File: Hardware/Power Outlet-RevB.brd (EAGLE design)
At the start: 138.4 x 100 mm, 38 parts, among them IC1 ATMega 328p-pu, IC2 ULN2003AD, K1 G5LE, K2 G5LE, Q1 8MHz, X1 VIN, X2 VOUT2, X3 VOUT1, X7 EARTH

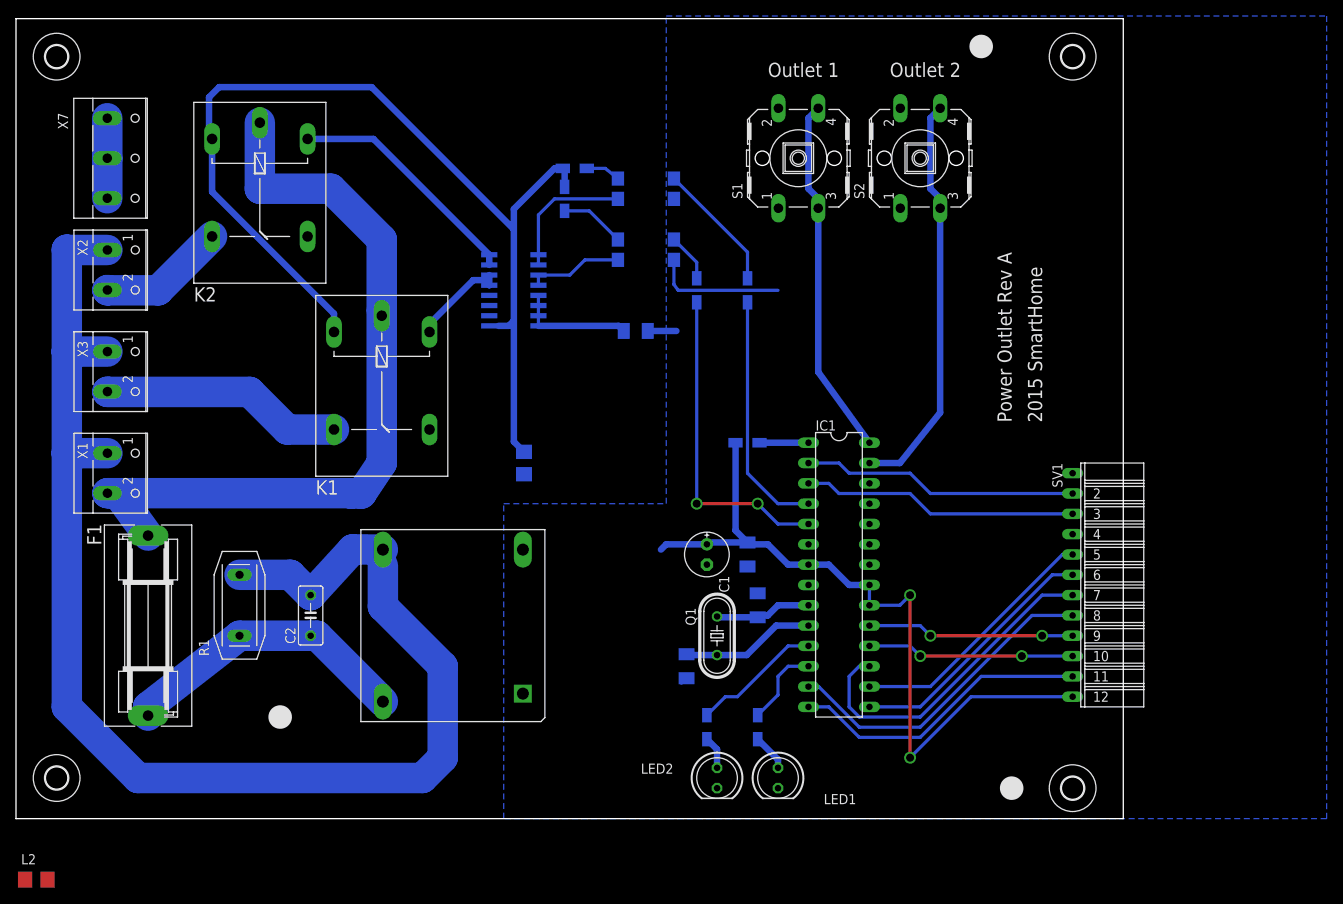
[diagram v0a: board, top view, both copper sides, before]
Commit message: updated wrong capacitor footprint, removed isolation cap as causes circuit not to function.
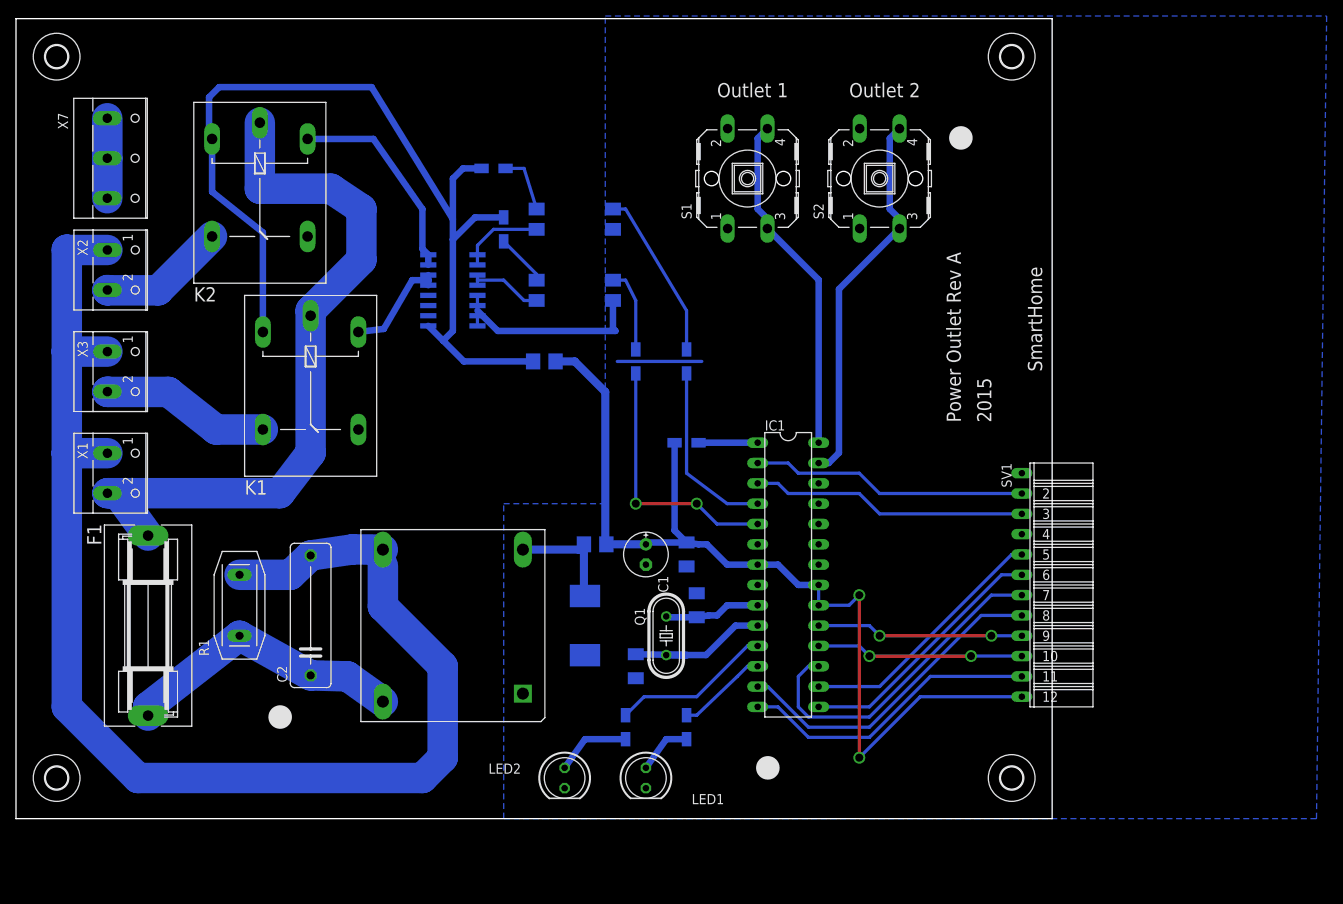
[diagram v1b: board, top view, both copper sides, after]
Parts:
- removed C6: 1n/2Kv, rcl:C1206K
- added D1: (no value), diode:SMC
- C2: device rcl:C050-030X075 -> rcl:C150-054X183
- OK1, OK2: device optocoupler:SMD4 -> optocoupler:DIL4-SMD
- moved L2 81.5 mm to (72.4, 34.3), flipped to the bottom
- moved LED2 19.0 mm to (68.6, 5.08)
- moved LED1 16.5 mm to (78.7, 5.08)
- moved L1 13.0 mm to (66.0, 57.1), turned to 0 degrees
- moved R5 11.7 mm to (83.8, 57.1)
- moved R6 11.7 mm to (77.5, 57.1)
- moved OK2 10.2 mm to (69.8, 66.0)
- moved R4 10.2 mm to (76.2, 11.4)
- moved R7 10.2 mm to (59.7, 81.3)
- moved OK1 9.67 mm to (69.8, 74.9)
- moved K1 8.89 mm to (36.8, 53.3)
- moved R3 8.89 mm to (83.8, 11.4)
- moved R8 8.52 mm to (61.0, 73.7)
- moved H2 7.73 mm to (124.5, 5.08)
- moved H3 7.62 mm to (124.5, 95.2)
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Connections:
- removed net AGND: C6.2, IC2.5, IC2.6, IC2.7, IC2.8
- net +3V3: now also D1.C
- net GND: now also D1.A, IC2.5, IC2.6, IC2.7, IC2.8; no longer C6.1
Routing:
- net +3V3: track 93.9 -> 135.1 mm
- net GND: track 20.9 -> 36.6 mm
- net AGND: track 14.7 -> 0.00 mm
- net N$14: track 30.3 -> 21.1 mm
- net N$1: track 98.8 -> 90.5 mm
- net OUT2_R: track 30.6 -> 22.6 mm
- net OUT1_R: track 40.2 -> 32.6 mm
- net VCC: track 126.6 -> 120.1 mm
- net N$17: track 17.0 -> 10.7 mm
- net N$8: track 4.11 -> 9.47 mm
- net N$6: track 16.8 -> 22.1 mm
- net N$15: track 16.3 -> 21.2 mm
- net N$16: track 6.03 -> 10.5 mm
- net OUT1_LED: track 16.3 -> 20.1 mm
- net N$12: track 30.0 -> 26.2 mm
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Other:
- board size 138.4 x 100 mm -> 129.5 x 100 mm
